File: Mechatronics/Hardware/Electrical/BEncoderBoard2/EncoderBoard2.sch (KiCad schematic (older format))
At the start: 43 parts, among them J1 Conn_01x08_Male, J2 Conn_01x07_Male, J6 Conn_01x04_Male, Q3 Q_PMOS_GSD, U1 STM32G431CBT6, U2 ITR1802, U3 ITR1802, U4 RN4871, Y1 8Mhz

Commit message: Changes
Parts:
- U2, U3: value ITR1802 -> ITR1802_Conn; footprint Encoder:OptointerrupterSmall -> Encoder:PinHeader_2x02_P2.54mm_Vertical
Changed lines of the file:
@@
 P 1500 1950
 F 0 "U2" H 1500 2275 50  0000 C CNN
-F 1 "ITR1802" H 1500 2184 50  0000 C CNN
-F 2 "Encoder:OptointerrupterSmall" H 1500 1950 50  0001 C CNN
+F 1 "ITR1802_Conn" H 1500 2184 50  0000 C CNN
+F 2 "Encoder:PinHeader_2x02_P2.54mm_Vertical" H 1500 1950 50  0001 C CNN
 F 3 "" H 1500 1950 50  0001 C CNN
 	1    1500 1950
@@
 P 1500 2850
 F 0 "U3" H 1500 3175 50  0000 C CNN
-F 1 "ITR1802" H 1500 3084 50  0000 C CNN
-F 2 "Encoder:OptointerrupterSmall" H 1500 2850 50  0001 C CNN
+F 1 "ITR1802_Conn" H 1500 2650 50  0000 C CNN
+F 2 "Encoder:PinHeader_2x02_P2.54mm_Vertical" H 1500 2850 50  0001 C CNN
 F 3 "" H 1500 2850 50  0001 C CNN
 	1    1500 2850

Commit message: Changed name
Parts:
- removed U2, U3: ITR1802_Conn, Encoder:PinHeader_2x02_P2.54mm_Vertical, symbol Encoder:ITR1802
- added U2, U3: ITR8102_Conn, Encoder:PinHeader_2x02_P2.54mm_Vertical, symbol Encoder:ITR8102
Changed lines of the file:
@@
 Comment4 ""
 $EndDescr
-$Comp
-L Encoder:ITR1802 U2
-U 1 1 5C28311C
-P 1500 1950
-F 0 "U2" H 1500 2275 50  0000 C CNN
-F 1 "ITR1802_Conn" H 1500 2184 50  0000 C CNN
-F 2 "Encoder:PinHeader_2x02_P2.54mm_Vertical" H 1500 1950 50  0001 C CNN
-F 3 "" H 1500 1950 50  0001 C CNN
-	1    1500 1950
-	1    0    0    -1
-$EndComp
-$Comp
-L Encoder:ITR1802 U3
-U 1 1 5C28324D
-P 1500 2850
-F 0 "U3" H 1500 3175 50  0000 C CNN
-F 1 "ITR1802_Conn" H 1500 2650 50  0000 C CNN
-F 2 "Encoder:PinHeader_2x02_P2.54mm_Vertical" H 1500 2850 50  0001 C CNN
-F 3 "" H 1500 2850 50  0001 C CNN
-	1    1500 2850
-	1    0    0    -1
-$EndComp
 Wire Wire Line
 	1200 2050 1200 2100
@@
 Wire Wire Line
 	4900 900  5450 900
+$Comp
+L Encoder:ITR8102 U3
+U 1 1 5F14F36F
+P 1500 2850
+F 0 "U3" H 1500 3100 50  0000 C CNN
+F 1 "ITR8102_Conn" H 1500 2650 50  0000 C CNN
+F 2 "Encoder:PinHeader_2x02_P2.54mm_Vertical" H 1500 2850 50  0001 C CNN
+F 3 "" H 1500 2850 50  0001 C CNN
+	1    1500 2850
+	1    0    0    -1
+$EndComp
+$Comp
+L Encoder:ITR8102 U2
+U 1 1 5F152A91
+P 1500 1950
+F 0 "U2" H 1500 2250 50  0000 C CNN
+F 1 "ITR8102_Conn" H 1500 2150 50  0000 C CNN
+F 2 "Encoder:PinHeader_2x02_P2.54mm_Vertical" H 1500 1950 50  0001 C CNN
+F 3 "" H 1500 1950 50  0001 C CNN
+	1    1500 1950
+	1    0    0    -1
+$EndComp
 $EndSCHEMATC

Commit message: Changed files
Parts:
- removed U2, U3: ITR8102_Conn, Encoder:PinHeader_2x02_P2.54mm_Vertical, symbol Encoder:ITR8102
- added U2, U3: OPTO_Conn, Encoder:PinHeader_2x02_P2.54mm_Vertical, symbol Encoder:OPTO_Conn
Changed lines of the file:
@@
 	4900 900  5450 900
 $Comp
-L Encoder:ITR8102 U3
-U 1 1 5F14F36F
+L Encoder:OPTO_Conn U3
+U 1 1 5F1557B4
 P 1500 2850
-F 0 "U3" H 1500 3100 50  0000 C CNN
-F 1 "ITR8102_Conn" H 1500 2650 50  0000 C CNN
+F 0 "U3" H 1500 3175 50  0000 C CNN
+F 1 "OPTO_Conn" H 1500 3084 50  0000 C CNN
 F 2 "Encoder:PinHeader_2x02_P2.54mm_Vertical" H 1500 2850 50  0001 C CNN
 F 3 "" H 1500 2850 50  0001 C CNN
@@
 $EndComp
 $Comp
-L Encoder:ITR8102 U2
-U 1 1 5F152A91
+L Encoder:OPTO_Conn U2
+U 1 1 5F15DEA7
 P 1500 1950
-F 0 "U2" H 1500 2250 50  0000 C CNN
-F 1 "ITR8102_Conn" H 1500 2150 50  0000 C CNN
+F 0 "U2" H 1500 2275 50  0000 C CNN
+F 1 "OPTO_Conn" H 1500 2184 50  0000 C CNN
 F 2 "Encoder:PinHeader_2x02_P2.54mm_Vertical" H 1500 1950 50  0001 C CNN
 F 3 "" H 1500 1950 50  0001 C CNN

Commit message: Changed files
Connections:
- wire segments 116 -> 118
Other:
- moved on the sheet: Q3, R1, R2, R3, R4, U2, U3
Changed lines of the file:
@@
 Comment4 ""
 $EndDescr
-Wire Wire Line
-	1200 2050 1200 2100
 $Comp
 L Device:R R1
 U 1 1 5C285A10
-P 1200 2250
-F 0 "R1" H 1270 2296 50  0000 L CNN
-F 1 "560" H 1270 2205 50  0000 L CNN
-F 2 "Encoder:R_0603_1608Metric_Pad1.05x0.95mm_HandSolder" V 1130 2250 50  0001 C CNN
-F 3 "~" H 1200 2250 50  0001 C CNN
-	1    1200 2250
+P 900 2300
+F 0 "R1" H 970 2346 50  0000 L CNN
+F 1 "560" H 970 2255 50  0000 L CNN
+F 2 "Encoder:R_0603_1608Metric_Pad1.05x0.95mm_HandSolder" V 830 2300 50  0001 C CNN
+F 3 "~" H 900 2300 50  0001 C CNN
+	1    900  2300
 	1    0    0    -1
 $EndComp
@@
 L Device:R R2
 U 1 1 5C285A71
-P 1200 3250
-F 0 "R2" V 1100 3150 50  0000 L CNN
-F 1 "560" V 1100 3300 50  0000 L CNN
-F 2 "Encoder:R_0603_1608Metric_Pad1.05x0.95mm_HandSolder" V 1130 3250 50  0001 C CNN
-F 3 "~" H 1200 3250 50  0001 C CNN
-	1    1200 3250
+P 900 3400
+F 0 "R2" H 950 3450 50  0000 L CNN
+F 1 "560" H 950 3350 50  0000 L CNN
+F 2 "Encoder:R_0603_1608Metric_Pad1.05x0.95mm_HandSolder" V 830 3400 50  0001 C CNN
+F 3 "~" H 900 3400 50  0001 C CNN
+	1    900  3400
 	1    0    0    -1
 $EndComp
@@
 L power:GND #PWR0110
 U 1 1 5C2863B3
-P 1200 2400
-F 0 "#PWR0110" H 1200 2150 50  0001 C CNN
-F 1 "GND" H 1205 2227 50  0000 C CNN
-F 2 "" H 1200 2400 50  0001 C CNN
-F 3 "" H 1200 2400 50  0001 C CNN
-	1    1200 2400
+P 900 2450
+F 0 "#PWR0110" H 900 2200 50  0001 C CNN
+F 1 "GND" H 905 2277 50  0000 C CNN
+F 2 "" H 900 2450 50  0001 C CNN
+F 3 "" H 900 2450 50  0001 C CNN
+	1    900  2450
 	1    0    0    -1
 $EndComp
@@
 L power:GND #PWR0112
 U 1 1 5C2895D3
-P 1900 1850
-F 0 "#PWR0112" H 1900 1600 50  0001 C CNN
-F 1 "GND" H 1905 1677 50  0000 C CNN
-F 2 "" H 1900 1850 50  0001 C CNN
-F 3 "" H 1900 1850 50  0001 C CNN
-	1    1900 1850
+P 1800 1850
+F 0 "#PWR0112" H 1800 1600 50  0001 C CNN
+F 1 "GND" H 1805 1677 50  0000 C CNN
+F 2 "" H 1800 1850 50  0001 C CNN
+F 3 "" H 1800 1850 50  0001 C CNN
+	1    1800 1850
 	-1   0    0    1
 $EndComp
@@
 L power:GND #PWR0113
 U 1 1 5C289611
-P 1900 2750
-F 0 "#PWR0113" H 1900 2500 50  0001 C CNN
-F 1 "GND" H 1905 2577 50  0000 C CNN
-F 2 "" H 1900 2750 50  0001 C CNN
-F 3 "" H 1900 2750 50  0001 C CNN
-	1    1900 2750
-	-1   0    0    1
-$EndComp
-Wire Wire Line
-	1800 1850 1900 1850
-Wire Wire Line
-	1900 2750 1800 2750
+P 1800 2950
+F 0 "#PWR0113" H 1800 2700 50  0001 C CNN
+F 1 "GND" H 1805 2777 50  0000 C CNN
+F 2 "" H 1800 2950 50  0001 C CNN
+F 3 "" H 1800 2950 50  0001 C CNN
+	1    1800 2950
+	-1   0    0    1
+$EndComp
+Wire Wire Line
+	1600 1850 1800 1850
+Wire Wire Line
+	1800 2950 1600 2950
 $Comp
 L Device:R R3
 U 1 1 5C28C76B
-P 2050 1900
-F 0 "R3" H 2120 1946 50  0000 L CNN
-F 1 "1.2K" H 2120 1855 50  0000 L CNN
-F 2 "Encoder:R_0603_1608Metric_Pad1.05x0.95mm_HandSolder" V 1980 1900 50  0001 C CNN
-F 3 "~" H 2050 1900 50  0001 C CNN
-	1    2050 1900
-	1    0    0    -1
-$EndComp
-Text Label 2250 2050 0    50   ~ 0
+P 1950 1900
+F 0 "R3" H 2020 1946 50  0000 L CNN
+F 1 "1.2K" H 2020 1855 50  0000 L CNN
+F 2 "Encoder:R_0603_1608Metric_Pad1.05x0.95mm_HandSolder" V 1880 1900 50  0001 C CNN
+F 3 "~" H 1950 1900 50  0001 C CNN
+	1    1950 1900
+	1    0    0    -1
+$EndComp
+Text Label 2150 2050 0    50   ~ 0
 SIGB
 Wire Wire Line
-	1800 2050 2050 2050
-Wire Wire Line
-	2050 2050 2450 2050
-Connection ~ 2050 2050
+	1600 2050 1950 2050
+Wire Wire Line
+	1950 2050 2350 2050
+Connection ~ 1950 2050
 $Comp
 L Device:R R4
 U 1 1 5C293966
-P 2050 2800
-F 0 "R4" H 2120 2846 50  0000 L CNN
-F 1 "1.2K" H 2120 2755 50  0000 L CNN
-F 2 "Encoder:R_0603_1608Metric_Pad1.05x0.95mm_HandSolder" V 1980 2800 50  0001 C CNN
-F 3 "~" H 2050 2800 50  0001 C CNN
-	1    2050 2800
-	1    0    0    -1
-$EndComp
-Wire Wire Line
-	1800 2950 2050 2950
-Wire Wire Line
-	2050 2950 2450 2950
-Connection ~ 2050 2950
-Text Label 2250 2950 0    50   ~ 0
+P 1950 3000
+F 0 "R4" H 2020 3046 50  0000 L CNN
+F 1 "1.2K" H 2020 2955 50  0000 L CNN
+F 2 "Encoder:R_0603_1608Metric_Pad1.05x0.95mm_HandSolder" V 1880 3000 50  0001 C CNN
+F 3 "~" H 1950 3000 50  0001 C CNN
+	1    1950 3000
+	1    0    0    -1
+$EndComp
+Wire Wire Line
+	1600 3150 1950 3150
+Wire Wire Line
+	1950 3150 2350 3150
+Connection ~ 1950 3150
+Text Label 2150 3150 0    50   ~ 0
 SIGA
 $Comp
 L Encoder:Q_PMOS_GSD Q3
 U 1 1 5D553268
-P 1350 1150
-F 0 "Q3" H 1450 950 50  0000 C CNN
-F 1 "Q_PMOS_GSD" H 1450 850 50  0000 C CNN
-F 2 "Encoder:SOT-23" V 1550 1000 50  0001 C CNN
-F 3 "~" V 1350 1200 50  0001 C CNN
-	1    1350 1150
-	1    0    0    -1
-$EndComp
-Text Label 1750 900  2    50   ~ 0
+P 1150 1150
+F 0 "Q3" H 1250 950 50  0000 C CNN
+F 1 "Q_PMOS_GSD" H 1250 850 50  0000 C CNN
+F 2 "Encoder:SOT-23" V 1350 1000 50  0001 C CNN
+F 3 "~" V 1150 1200 50  0001 C CNN
+	1    1150 1150
+	1    0    0    -1
+$EndComp
+Text Label 1550 900  2    50   ~ 0
 EncEnable
 Wire Wire Line
-	1750 900  1350 900
+	1550 900  1150 900
 $Comp
 L power:+3.3V #PWR017
 U 1 1 5D59FF5B
-P 1550 1200
-F 0 "#PWR017" H 1550 1050 50  0001 C CNN
-F 1 "+3.3V" H 1565 1373 50  0000 C CNN
-F 2 "" H 1550 1200 50  0001 C CNN
-F 3 "" H 1550 1200 50  0001 C CNN
-	1    1550 1200
-	1    0    0    -1
-$EndComp
-Wire Wire Line
-	2050 1750 2050 1550
-Wire Wire Line
-	2050 2650 2550 2650
-Wire Wire Line
-	2550 2650 2550 1550
-Wire Wire Line
-	2550 1550 2050 1550
-Connection ~ 2050 1550
-Wire Wire Line
-	1050 2750 1050 1850
-Wire Wire Line
-	1050 1200 1150 1200
-Wire Wire Line
-	1050 2750 1200 2750
-Wire Wire Line
-	1050 1550 2050 1550
-Connection ~ 1050 1550
-Wire Wire Line
-	1050 1550 1050 1200
-Wire Wire Line
-	1050 1850 1200 1850
-Connection ~ 1050 1850
-Wire Wire Line
-	1050 1850 1050 1550
+P 1350 1200
+F 0 "#PWR017" H 1350 1050 50  0001 C CNN
+F 1 "+3.3V" H 1365 1373 50  0000 C CNN
+F 2 "" H 1350 1200 50  0001 C CNN
+F 3 "" H 1350 1200 50  0001 C CNN
+	1    1350 1200
+	1    0    0    -1
+$EndComp
+Wire Wire Line
+	1950 1750 1950 1550
+Wire Wire Line
+	1950 2850 2450 2850
+Wire Wire Line
+	2450 2850 2450 1550
+Wire Wire Line
+	2450 1550 1950 1550
+Connection ~ 1950 1550
+Wire Wire Line
+	750  2950 750  1850
+Wire Wire Line
+	750  1200 950  1200
+Wire Wire Line
+	750  2950 1000 2950
+Wire Wire Line
+	750  1550 1950 1550
+Connection ~ 750  1550
+Wire Wire Line
+	750  1550 750  1200
+Wire Wire Line
+	750  1850 1000 1850
+Connection ~ 750  1850
+Wire Wire Line
+	750  1850 750  1550
 $Comp
 L Encoder:RN4871 U4
@@
 L power:GND #PWR0128
 U 1 1 5F196248
-P 1200 3400
-F 0 "#PWR0128" H 1200 3150 50  0001 C CNN
-F 1 "GND" H 1205 3227 50  0000 C CNN
-F 2 "" H 1200 3400 50  0001 C CNN
-F 3 "" H 1200 3400 50  0001 C CNN
-	1    1200 3400
-	1    0    0    -1
-$EndComp
-Wire Wire Line
-	1200 3100 1200 2950
+P 900 3550
+F 0 "#PWR0128" H 900 3300 50  0001 C CNN
+F 1 "GND" H 905 3377 50  0000 C CNN
+F 2 "" H 900 3550 50  0001 C CNN
+F 3 "" H 900 3550 50  0001 C CNN
+	1    900  3550
+	1    0    0    -1
+$EndComp
 Wire Wire Line
 	5450 1200 5100 1200
@@
 L Encoder:OPTO_Conn U3
 U 1 1 5F1557B4
-P 1500 2850
-F 0 "U3" H 1500 3175 50  0000 C CNN
-F 1 "OPTO_Conn" H 1500 3084 50  0000 C CNN
-F 2 "Encoder:PinHeader_2x02_P2.54mm_Vertical" H 1500 2850 50  0001 C CNN
-F 3 "" H 1500 2850 50  0001 C CNN
-	1    1500 2850
+P 1300 3050
+F 0 "U3" H 1300 3350 50  0000 C CNN
+F 1 "OPTO_Conn" H 1300 3250 50  0000 C CNN
+F 2 "Encoder:PinHeader_2x02_P2.54mm_Vertical" H 1300 3050 50  0001 C CNN
+F 3 "" H 1300 3050 50  0001 C CNN
+	1    1300 3050
 	1    0    0    -1
 $EndComp
@@
 L Encoder:OPTO_Conn U2
 U 1 1 5F15DEA7
-P 1500 1950
-F 0 "U2" H 1500 2275 50  0000 C CNN
-F 1 "OPTO_Conn" H 1500 2184 50  0000 C CNN
-F 2 "Encoder:PinHeader_2x02_P2.54mm_Vertical" H 1500 1950 50  0001 C CNN
-F 3 "" H 1500 1950 50  0001 C CNN
-	1    1500 1950
-	1    0    0    -1
-$EndComp
+P 1300 1950
+F 0 "U2" H 1300 2275 50  0000 C CNN
+F 1 "OPTO_Conn" H 1300 2150 50  0000 C CNN
+F 2 "Encoder:PinHeader_2x02_P2.54mm_Vertical" H 1300 1950 50  0001 C CNN
+F 3 "" H 1300 1950 50  0001 C CNN
+	1    1300 1950
+	1    0    0    -1
+$EndComp
+Wire Wire Line
+	900  2150 900  2050
+Wire Wire Line
+	900  2050 1000 2050
+Wire Wire Line
+	900  3250 900  3150
+Wire Wire Line
+	900  3150 1000 3150
 $EndSCHEMATC

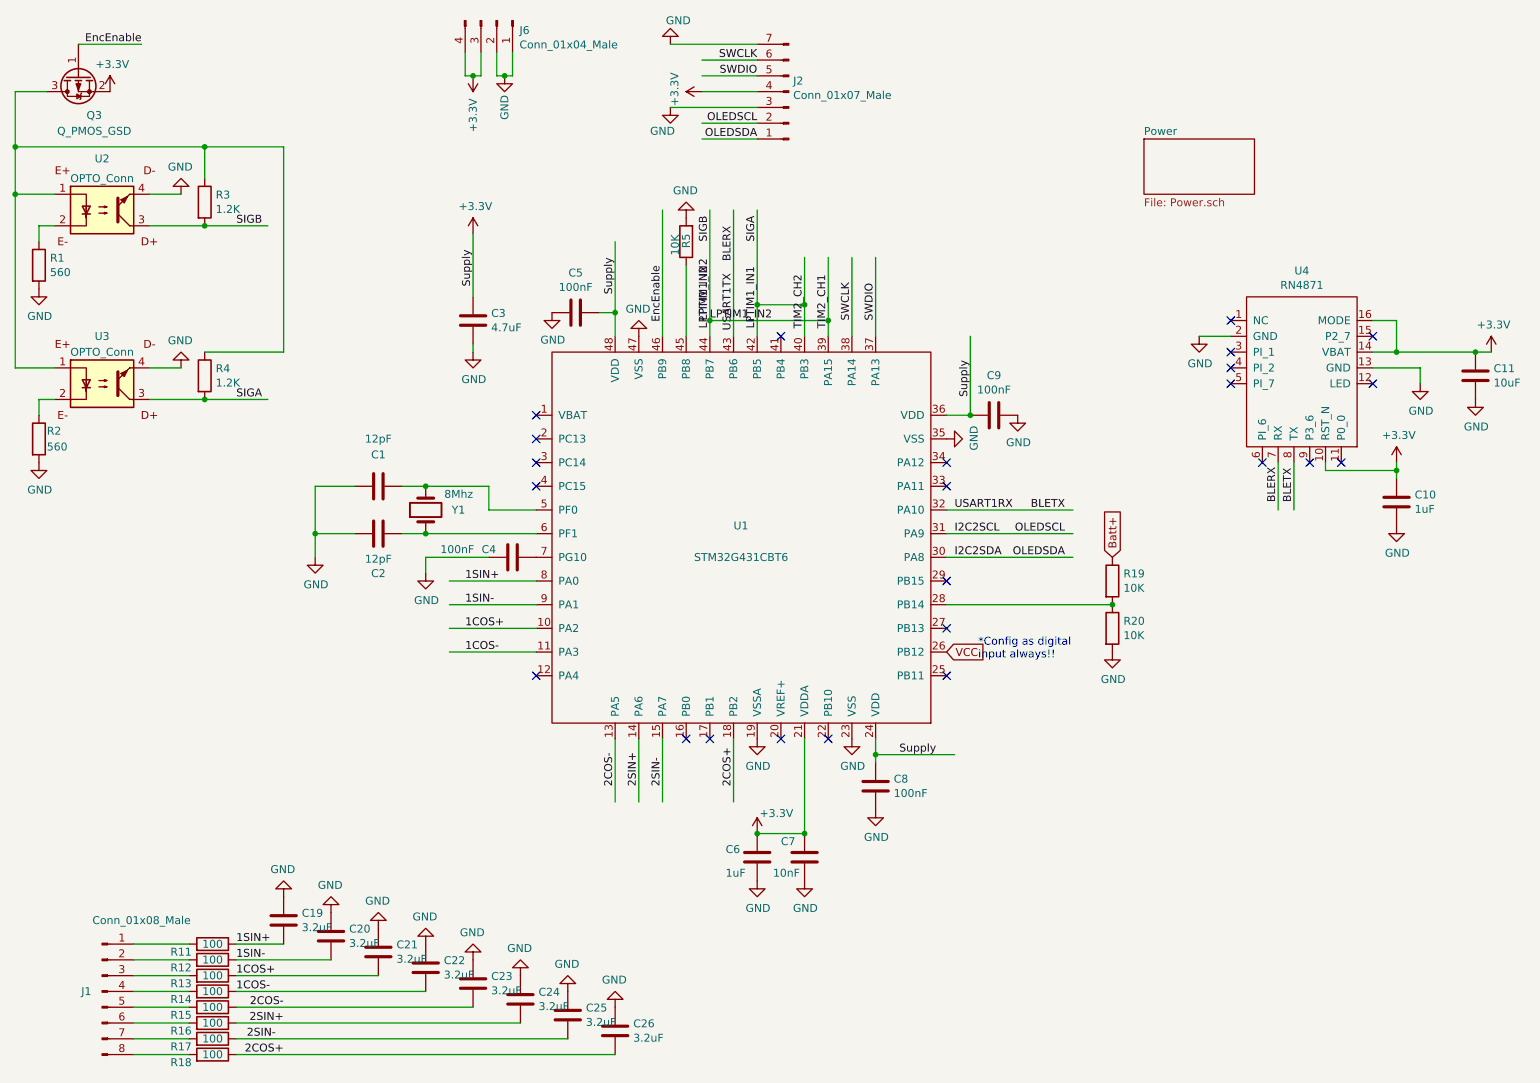
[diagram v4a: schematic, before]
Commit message: pin header change
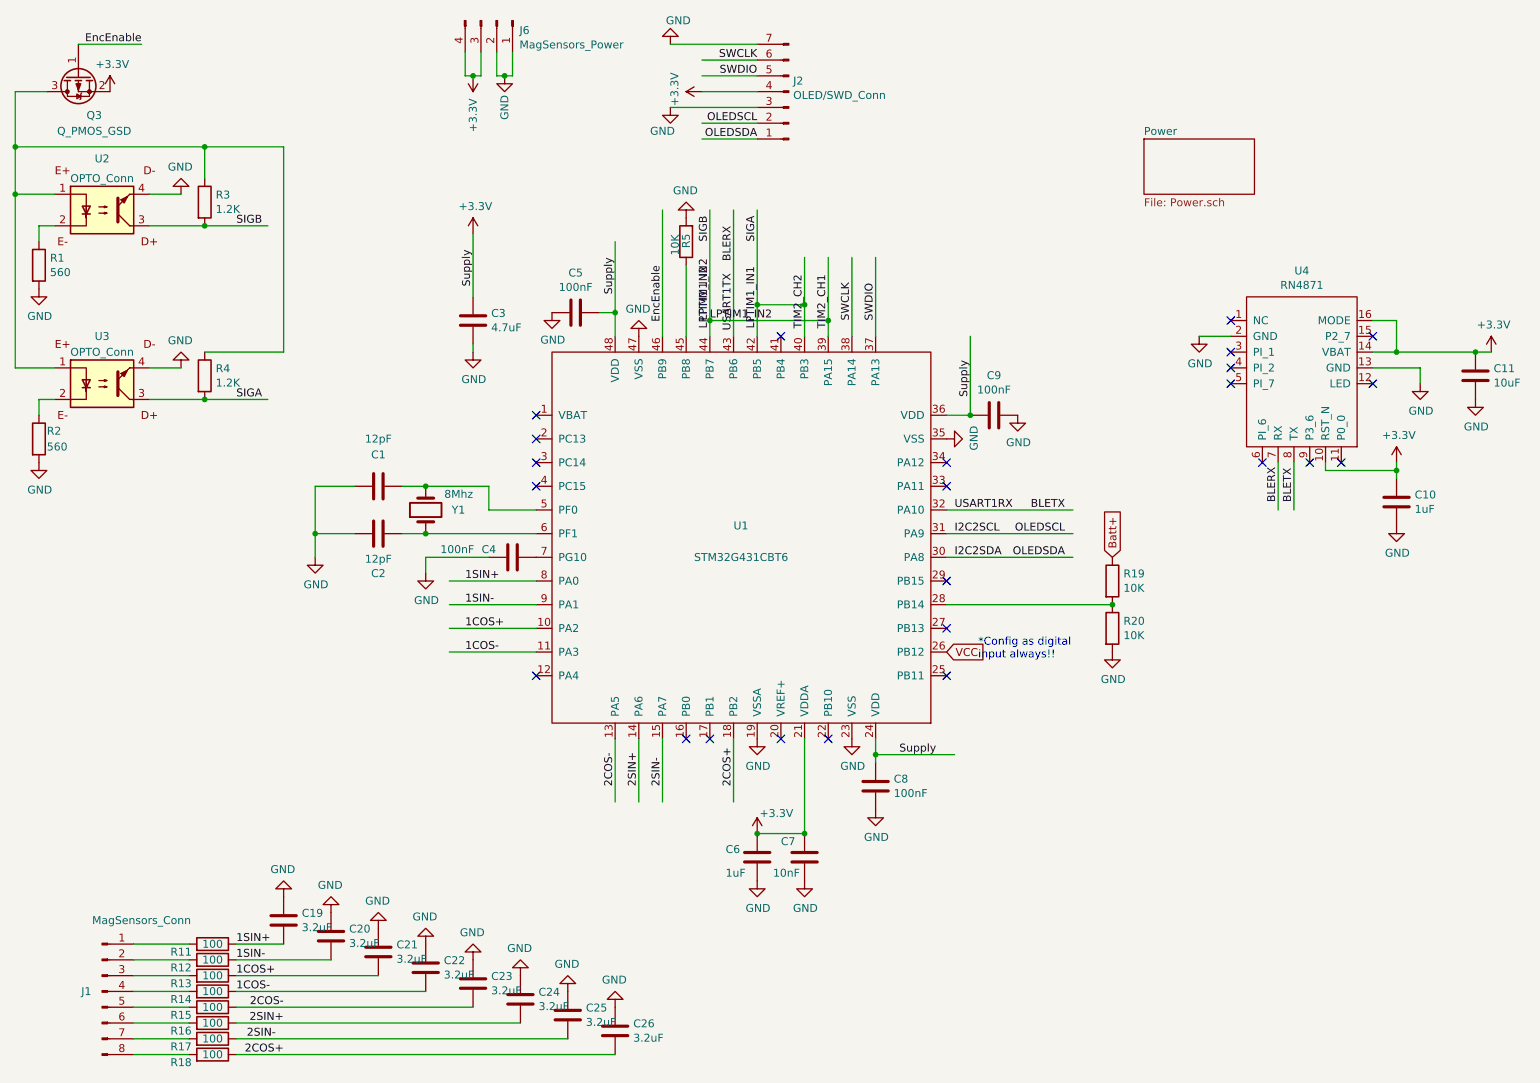
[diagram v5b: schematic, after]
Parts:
- J1: value Conn_01x08_Male -> MagSensors_Conn
- J2: value Conn_01x07_Male -> OLED/SWD_Conn
- J6: value Conn_01x04_Male -> MagSensors_Power
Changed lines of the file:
@@
 P 1300 6900
 F 0 "J1" H 1200 6900 50  0000 C CNN
-F 1 "Conn_01x08_Male" H 1550 7350 50  0000 C CNN
+F 1 "MagSensors_Conn" H 1550 7350 50  0000 C CNN
 F 2 "Encoder:PinHeader_1x08_P2.54mm_Vertical" H 1300 6900 50  0001 C CNN
 F 3 "~" H 1300 6900 50  0001 C CNN
@@
 P 3800 750
 F 0 "J6" V 3862 894 50  0000 L CNN
-F 1 "Conn_01x04_Male" V 3953 894 50  0000 L CNN
+F 1 "MagSensors_Power" V 3953 894 50  0000 L CNN
 F 2 "Encoder:PinHeader_2x02_P2.54mm_Vertical" H 3800 750 50  0001 C CNN
 F 3 "~" H 3800 750 50  0001 C CNN
@@
 P 5650 1200
 F 0 "J2" H 5622 1132 50  0000 R CNN
-F 1 "Conn_01x07_Male" H 5622 1223 50  0000 R CNN
+F 1 "OLED/SWD_Conn" H 5622 1223 50  0000 R CNN
 F 2 "Encoder:PinHeader_1x07_P2.54mm_Vertical" H 5650 1200 50  0001 C CNN
 F 3 "~" H 5650 1200 50  0001 C CNN
